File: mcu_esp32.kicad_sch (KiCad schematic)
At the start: 0 parts

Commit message: added components
servo controller, esp32
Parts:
- added C14: 100u, Capacitor_SMD:C_0805_2012Metric, symbol Device:C_Small
- added C15, C17, C20: 0.1u, Capacitor_SMD:C_0805_2012Metric, symbol Device:C_Small
- added C16, C19: 10u, Capacitor_SMD:C_0805_2012Metric, symbol Device:C_Small
- added C18, C21, C22: 1n / 50V, Capacitor_SMD:C_0805_2012Metric, symbol Device:C_Small
- added R10: 12k, Resistor_SMD:R_0805_2012Metric, symbol Device:R_Small
- added R11, R12, R9: 470R, Resistor_SMD:R_0805_2012Metric, symbol Device:R_Small
- added R13, R14: 12K, Resistor_SMD:R_0805_2012Metric, symbol Device:R_Small
- added R15, R16: 0R, Resistor_SMD:R_0805_2012Metric, symbol Device:R_Small
- added R17: 0R (NC), Resistor_SMD:R_0805_2012Metric, symbol Device:R_Small
- added R18: 0R(NC), Resistor_SMD:R_0805_2012Metric, symbol Device:R_Small
- added R8: 5K, Resistor_SMD:R_0805_2012Metric, symbol Device:R_Small
- added SW2, SW3: IO0, symbol Switch:SW_Push
- added T1, T2: S8050, symbol PCM_Elektuur:T-BJT-NPN
- added U5: CP2102N-Axx-xQFN28, Package_DFN_QFN:QFN-28-1EP_5x5mm_P0.5mm_EP3.1x3.1mm_ThermalVias, symbol Interface_USB:CP2102N-Axx-xQFN28
- added U6: ESP32-WROOM-32D, RF_Module:ESP32-WROOM-32D, symbol RF_Module:ESP32-WROOM-32D
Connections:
- new net: C21.1, R11.2, SW2.2
- new net: C22.1, R12.2, SW3.2
- new net: R14.1, T2.2 (B)
- new net: R9.2, U5.26 (TXD)
- new net: R13.1, T1.2 (B)
- new net 3V3: C14.2, C15.2, C16.1, C17.1, R10.2, R8.1, U5.6 (VDD), U5.7 (VREGIN), U6.2 (VDD)
- new net 5V1: C19.2, C20.2, U5.8 (VBUS)
- new net CTS: R18.1, U5.23 (~{CTS})
- new net DSR: U5.27 (~{DSR})
- new net DTR: R13.2, T2.3 (E), U5.28 (~{DTR})
- new net EN: C18.2, R10.1, R12.1, T1.1 (C), U6.3 (EN)
- new net ESP_D+: U5.4 (D+)
- new net ESP_D-: U5.5 (D-)
- new net GND: C14.1, C15.1, C16.2, C17.2, C18.1, C19.1, C20.1, C21.2, C22.2, SW2.1, SW3.1, U5.29 (GND), U5.3 (GND), U6.1 (GND), U6.15 (GND), U6.38 (GND), U6.39 (GND)
- new net IO0: R11.1, R8.2, T2.1 (C), U6.25 (IO0)
- new net IO13: R18.2, U6.16 (IO13)
- new net IO15: R17.2, U6.23 (IO15)
- new net IO23: U6.37 (IO23)
- new net RTS: R14.2, R17.1, T1.3 (E), U5.24 (~{RTS})
- new net RXD: R16.1, U5.25 (RXD)
- new net RXD0: R15.2, U6.34 (RXD0/IO3)
- new net SENSOR_VN: U6.5 (SENSOR_VN)
- new net SENSOR_VP: U6.4 (SENSOR_VP)
- new net TXD: R15.1, R9.1
- new net TXD0: R16.2, U6.35 (TXD0/IO1)
- no-connect marks 0 -> 1

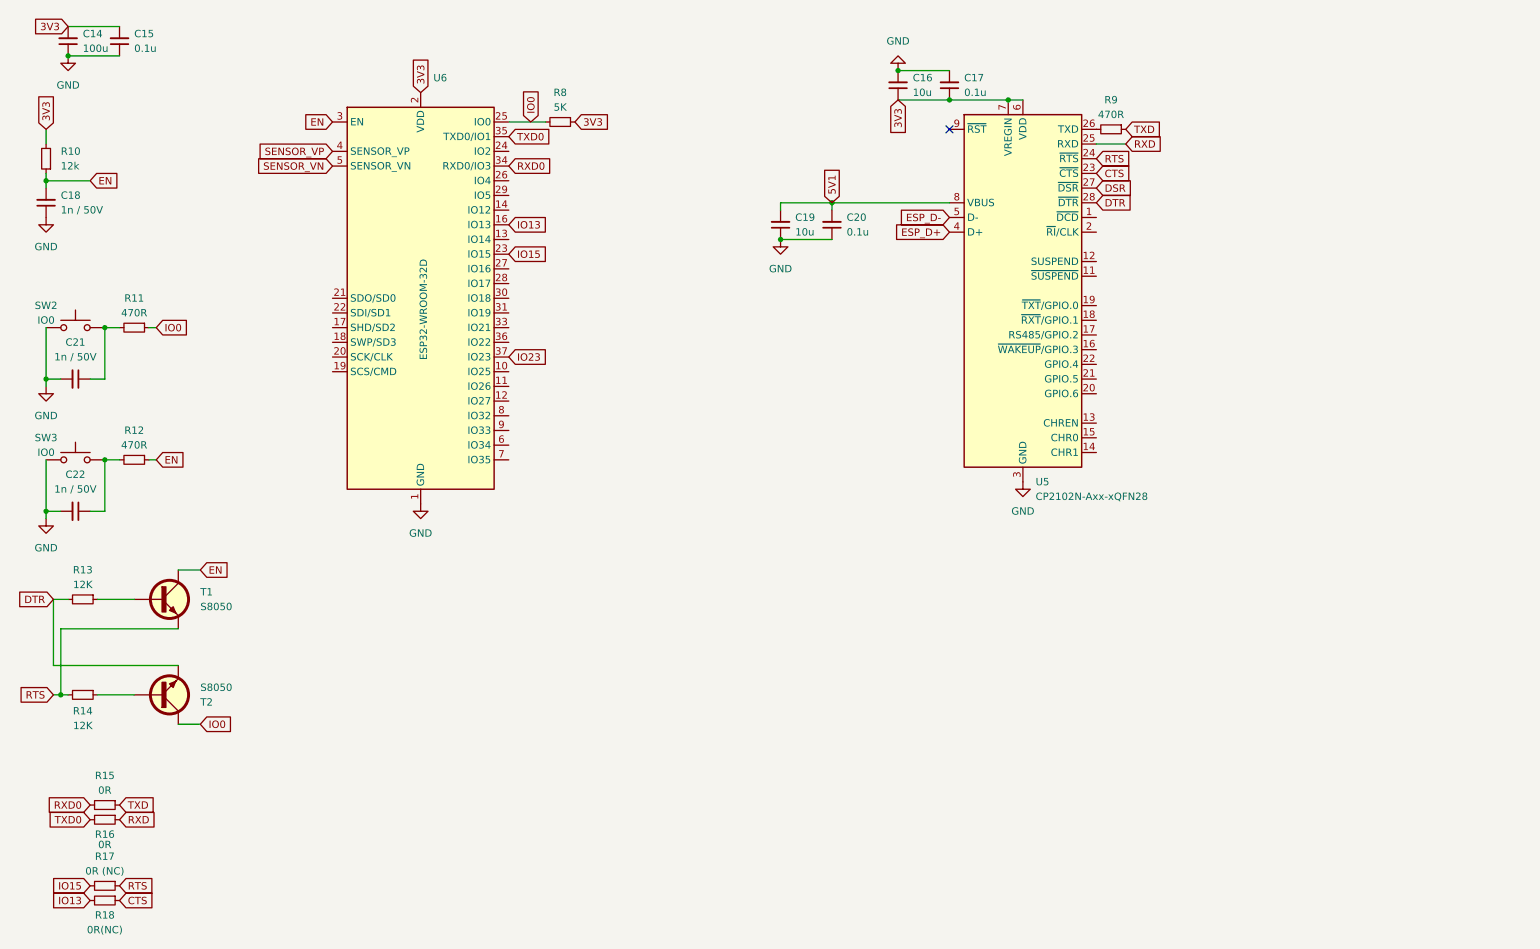
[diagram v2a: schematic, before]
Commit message: gpio expander added comm finished
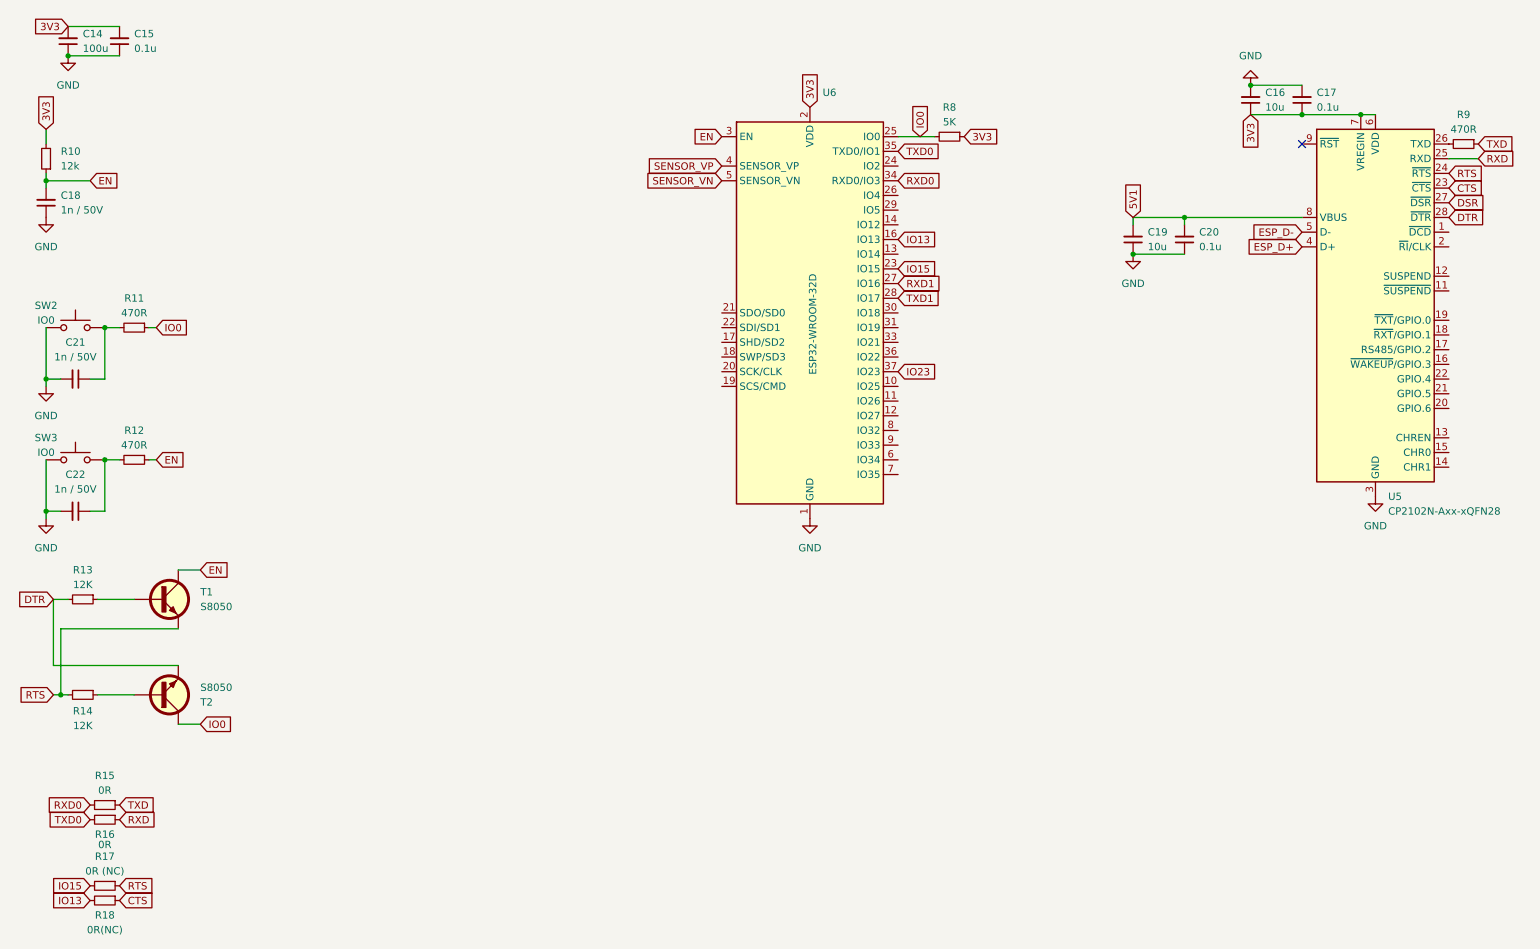
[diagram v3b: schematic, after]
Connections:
- net RXD1: now reaches U6.27 (IO16)
- net TXD1: now reaches U6.28 (IO17)
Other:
- moved on the sheet: C16, C17, C19, C20, R8, R9, U5, U6

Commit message: Visual Improvements
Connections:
- net DSR: no longer names the net of U5.27 (~{DSR})
- net SENSOR_VN: no longer names the net of U6.5 (SENSOR_VN)
- net SENSOR_VP: no longer names the net of U6.4 (SENSOR_VP)
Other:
- note added: "Auto Download"
- note added: "ESP32"
- note added: "ESP32 Power Decoupling Caps"
- note added: "External Reset Button"
- note added: "Mode Selection"
- note added: "UART to USB"
- moved on the sheet: C14, C15, C16, C17, C18, C19, C20, C21, C22, R10, R11, R12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

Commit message: schematic finished
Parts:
- SW2: footprint (none) -> Button_Switch_SMD:SW_SPST_B3U-1000P
- SW3: value IO0 -> EN; footprint (none) -> Button_Switch_SMD:SW_SPST_B3U-1000P
- T1, T2: footprint (none) -> Package_TO_SOT_SMD:TSOT-23
- renumbered R9 to R10, R13 to R12, R14 to R13, R12 to R14, R10 to R9, U6 to U5, U5 to U6
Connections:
- net IO23: no longer names the net of U5.37 (IO23)
- no-connect marks 1 -> 7
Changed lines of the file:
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@@
 	)
 	(no_connect
+		(at 214.63 40.64)
+	)
+	(no_connect
+		(at 214.63 45.72)
+	)
+	(no_connect
+		(at 21.59 35.56)
+	)
+	(no_connect
+		(at 52.07 86.36)
+	)
+	(no_connect
+		(at 52.07 83.82)
+	)
+	(no_connect
 		(at 189.23 30.48)
 	)
+	(no_connect
+		(at 21.59 33.02)
+	)
 	(wire
 		(pts
@@
 		)
 	)
-	(global_label "IO23"
-		(shape input)
-		(at 52.07 68.58 0)
-		(fields_autoplaced yes)
-		(effects
-			(font
-				(size 1.27 1.27)
-			)
-			(justify left)
-		)
-		(property "Intersheetrefs" "${INTERSHEET_REFS}"
-			(at 59.4095 68.58 0)
-			(effects
-				(font
-					(size 1.27 1.27)
-				)
-				(justify left)
-				(hide yes)
-			)
-		)
-	)
 	(symbol
 		(lib_id "power:GND")
@@
 		(dnp no)
 		(fields_autoplaced yes)
-		(property "Reference" "#PWR022"
+		(property "Reference" "#PWR021"
 			(at 78.74 62.23 0)
 			(effects
@@
 			(project "controllerForVehicle"
 				(path "/f177fb06-71dc-4865-9331-a828b12c2bf7/0ded9e45-71e1-4118-a2b1-0d1586a9cfb7"
-					(reference "#PWR022")
+					(reference "#PWR021")
 					(unit 1)
 				)
@@
 		(dnp no)
 		(fields_autoplaced yes)
-		(property "Reference" "#PWR025"
+		(property "Reference" "#PWR022"
 			(at 78.74 88.9 0)
 			(effects
@@
 			(project "controllerForVehicle"
 				(path "/f177fb06-71dc-4865-9331-a828b12c2bf7/0ded9e45-71e1-4118-a2b1-0d1586a9cfb7"
-					(reference "#PWR025")
+					(reference "#PWR022")
 					(unit 1)
 				)
@@
 		(dnp no)
 		(fields_autoplaced yes)
-		(property "Reference" "R10"
+		(property "Reference" "R9"
 			(at 130.81 29.2099 0)
 			(effects
@@
 			(project "controllerForVehicle"
 				(path "/f177fb06-71dc-4865-9331-a828b12c2bf7/0ded9e45-71e1-4118-a2b1-0d1586a9cfb7"
-					(reference "R10")
+					(reference "R9")
 					(unit 1)
 				)
@@
 		(dnp no)
 		(fields_autoplaced yes)
-		(property "Reference" "#PWR021"
+		(property "Reference" "#PWR020"
 			(at 160.02 55.88 0)
 			(effects
@@
 			(project "controllerForVehicle"
 				(path "/f177fb06-71dc-4865-9331-a828b12c2bf7/0ded9e45-71e1-4118-a2b1-0d1586a9cfb7"
-					(reference "#PWR021")
+					(reference "#PWR020")
 					(unit 1)
 				)
@@
 		(dnp no)
 		(fields_autoplaced yes)
-		(property "Reference" "R12"
+		(property "Reference" "R14"
 			(at 93.98 67.31 90)
 			(effects
@@
 			(project "controllerForVehicle"
 				(path "/f177fb06-71dc-4865-9331-a828b12c2bf7/0ded9e45-71e1-4118-a2b1-0d1586a9cfb7"
-					(reference "R12")
+					(reference "R14")
 					(unit 1)
 				)
@@
 		(on_board yes)
 		(dnp no)
-		(property "Reference" "U6"
+		(property "Reference" "U5"
 			(at 39.0241 20.32 0)
 			(effects
@@
 			(project ""
 				(path "/f177fb06-71dc-4865-9331-a828b12c2bf7/0ded9e45-71e1-4118-a2b1-0d1586a9cfb7"
-					(reference "U6")
+					(reference "U5")
 					(unit 1)
 				)
@@
 			)
 		)
-		(property "Footprint" ""
+		(property "Footprint" "Package_TO_SOT_SMD:TSOT-23"
 			(at 137.16 71.12 0)
 			(effects
@@
 		(dnp no)
 		(fields_autoplaced yes)
-		(property "Reference" "R9"
+		(property "Reference" "R10"
 			(at 217.17 25.4 90)
 			(effects
@@
 			(project "controllerForVehicle"
 				(path "/f177fb06-71dc-4865-9331-a828b12c2bf7/0ded9e45-71e1-4118-a2b1-0d1586a9cfb7"
-					(reference "R9")
+					(reference "R10")
 					(unit 1)
 				)
@@
 		(on_board yes)
 		(dnp no)
-		(property "Reference" "R14"
+		(property "Reference" "R13"
 			(at 123.19 73.914 90)
 			(effects
@@
 			(project "controllerForVehicle"
 				(path "/f177fb06-71dc-4865-9331-a828b12c2bf7/0ded9e45-71e1-4118-a2b1-0d1586a9cfb7"
-					(reference "R14")
+					(reference "R13")
 					(unit 1)
 				)
@@
 		(dnp no)
 		(fields_autoplaced yes)
-		(property "Reference" "R13"
+		(property "Reference" "R12"
 			(at 123.19 49.53 90)
 			(effects
@@
 			(project "controllerForVehicle"
 				(path "/f177fb06-71dc-4865-9331-a828b12c2bf7/0ded9e45-71e1-4118-a2b1-0d1586a9cfb7"
-					(reference "R13")
+					(reference "R12")
 					(unit 1)
 				)
@@
 		(dnp no)
 		(fields_autoplaced yes)
-		(property "Reference" "#PWR020"
+		(property "Reference" "#PWR019"
 			(at 128.27 46.99 0)
 			(effects
@@
 			(project "controllerForVehicle"
 				(path "/f177fb06-71dc-4865-9331-a828b12c2bf7/0ded9e45-71e1-4118-a2b1-0d1586a9cfb7"
-					(reference "#PWR020")
+					(reference "#PWR019")
 					(unit 1)
 				)
@@
 			)
 		)
-		(property "Footprint" ""
+		(property "Footprint" "Button_Switch_SMD:SW_SPST_B3U-1000P"
 			(at 83.82 40.64 0)
 			(effects
@@
 			)
 		)
-		(property "Footprint" ""
+		(property "Footprint" "Package_TO_SOT_SMD:TSOT-23"
 			(at 137.16 54.61 0)
 			(effects
@@
 			)
 		)
-		(property "Value" "IO0"
+		(property "Value" "EN"
 			(at 78.74 71.12 0)
 			(effects
@@
 			)
 		)
-		(property "Footprint" ""
+		(property "Footprint" "Button_Switch_SMD:SW_SPST_B3U-1000P"
 			(at 83.82 67.31 0)
 			(effects
@@
 		(dnp no)
 		(fields_autoplaced yes)
-		(property "Reference" "#PWR019"
+		(property "Reference" "#PWR017"
 			(at 180.34 13.97 0)
 			(effects
@@
 			(project "controllerForVehicle"
 				(path "/f177fb06-71dc-4865-9331-a828b12c2bf7/0ded9e45-71e1-4118-a2b1-0d1586a9cfb7"
-					(reference "#PWR019")
+					(reference "#PWR017")
 					(unit 1)
 				)
@@
 		(dnp no)
 		(fields_autoplaced yes)
-		(property "Reference" "U5"
+		(property "Reference" "U6"
 			(at 204.1241 91.44 0)
 			(effects
@@
 			(project ""
 				(path "/f177fb06-71dc-4865-9331-a828b12c2bf7/0ded9e45-71e1-4118-a2b1-0d1586a9cfb7"
-					(reference "U5")
+					(reference "U6")
 					(unit 1)
 				)

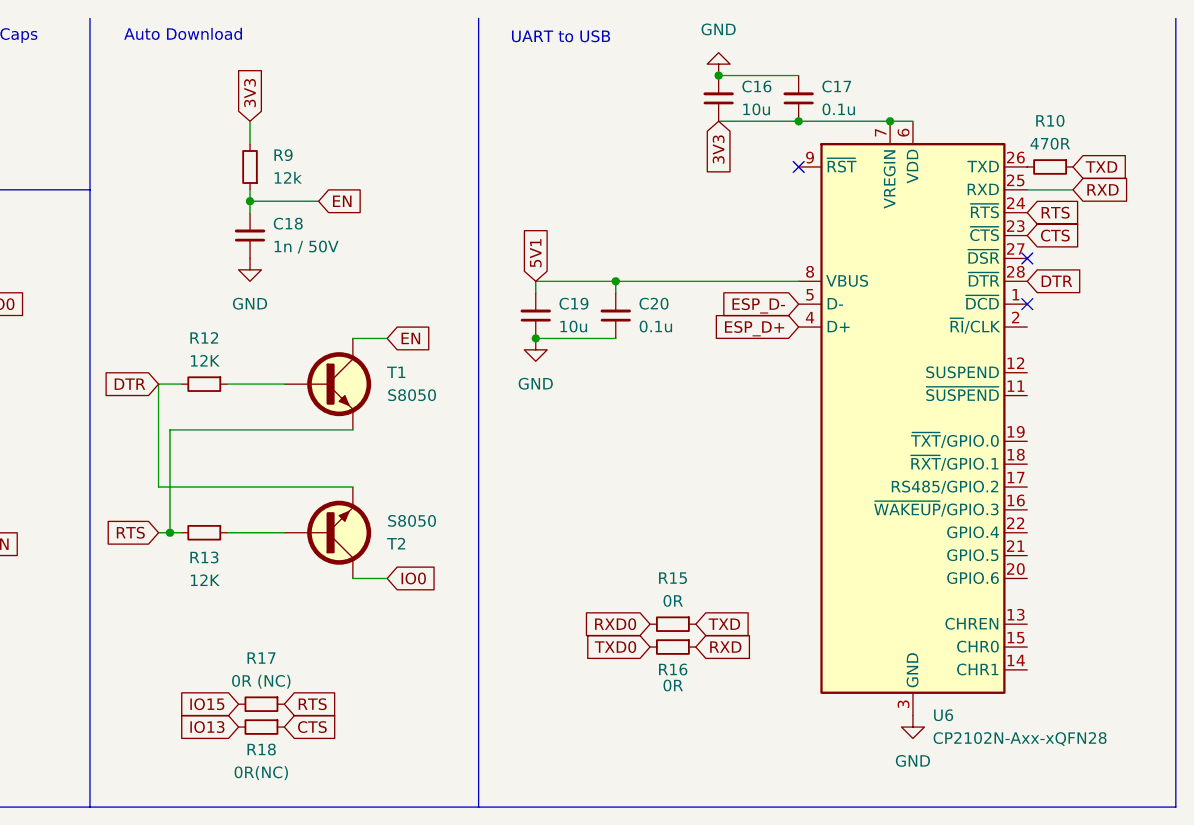
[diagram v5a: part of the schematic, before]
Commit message: Routing ESP32 and Components
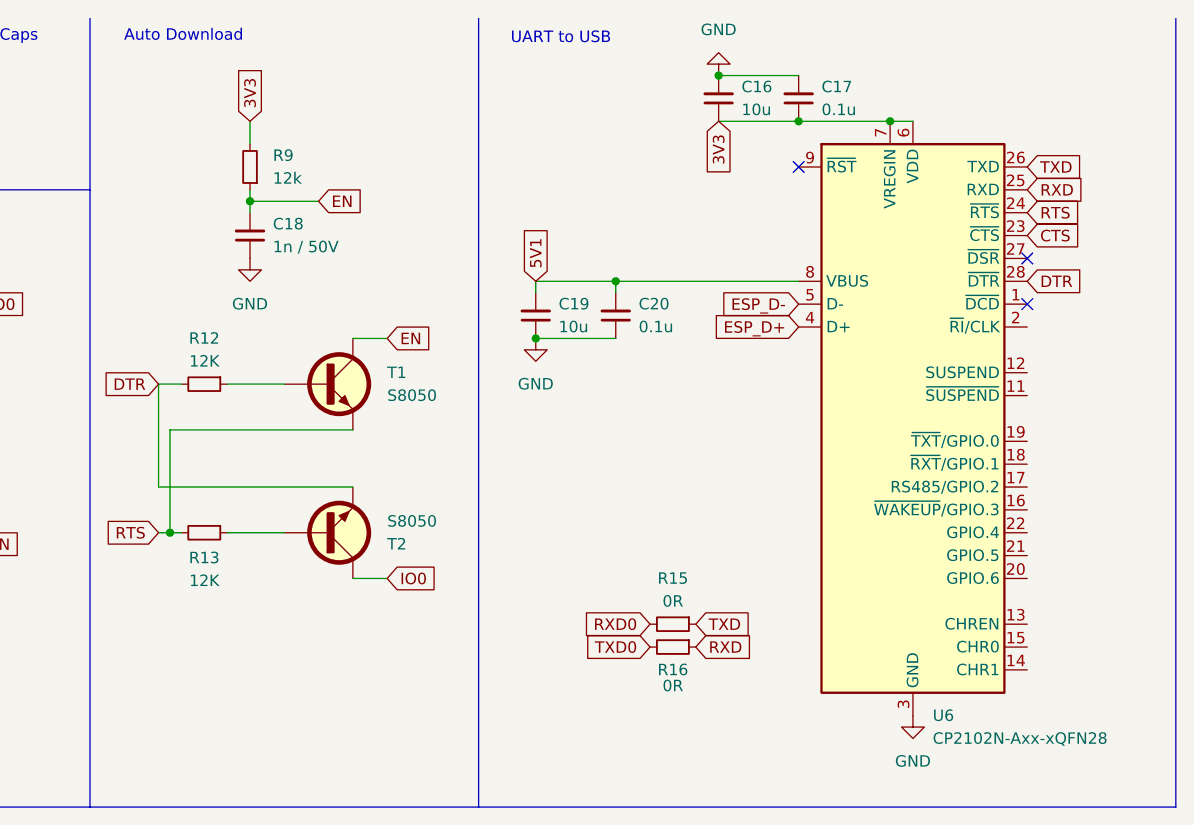
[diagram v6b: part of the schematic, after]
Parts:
- removed R10: 470R, Resistor_SMD:R_0805_2012Metric, symbol Device:R_Small
- removed R17: 0R (NC), Resistor_SMD:R_0805_2012Metric, symbol Device:R_Small
- removed R18: 0R(NC), Resistor_SMD:R_0805_2012Metric, symbol Device:R_Small
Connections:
- net TXD: now also U6.26 (TXD)
